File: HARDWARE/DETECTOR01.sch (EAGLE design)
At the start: 6 parts

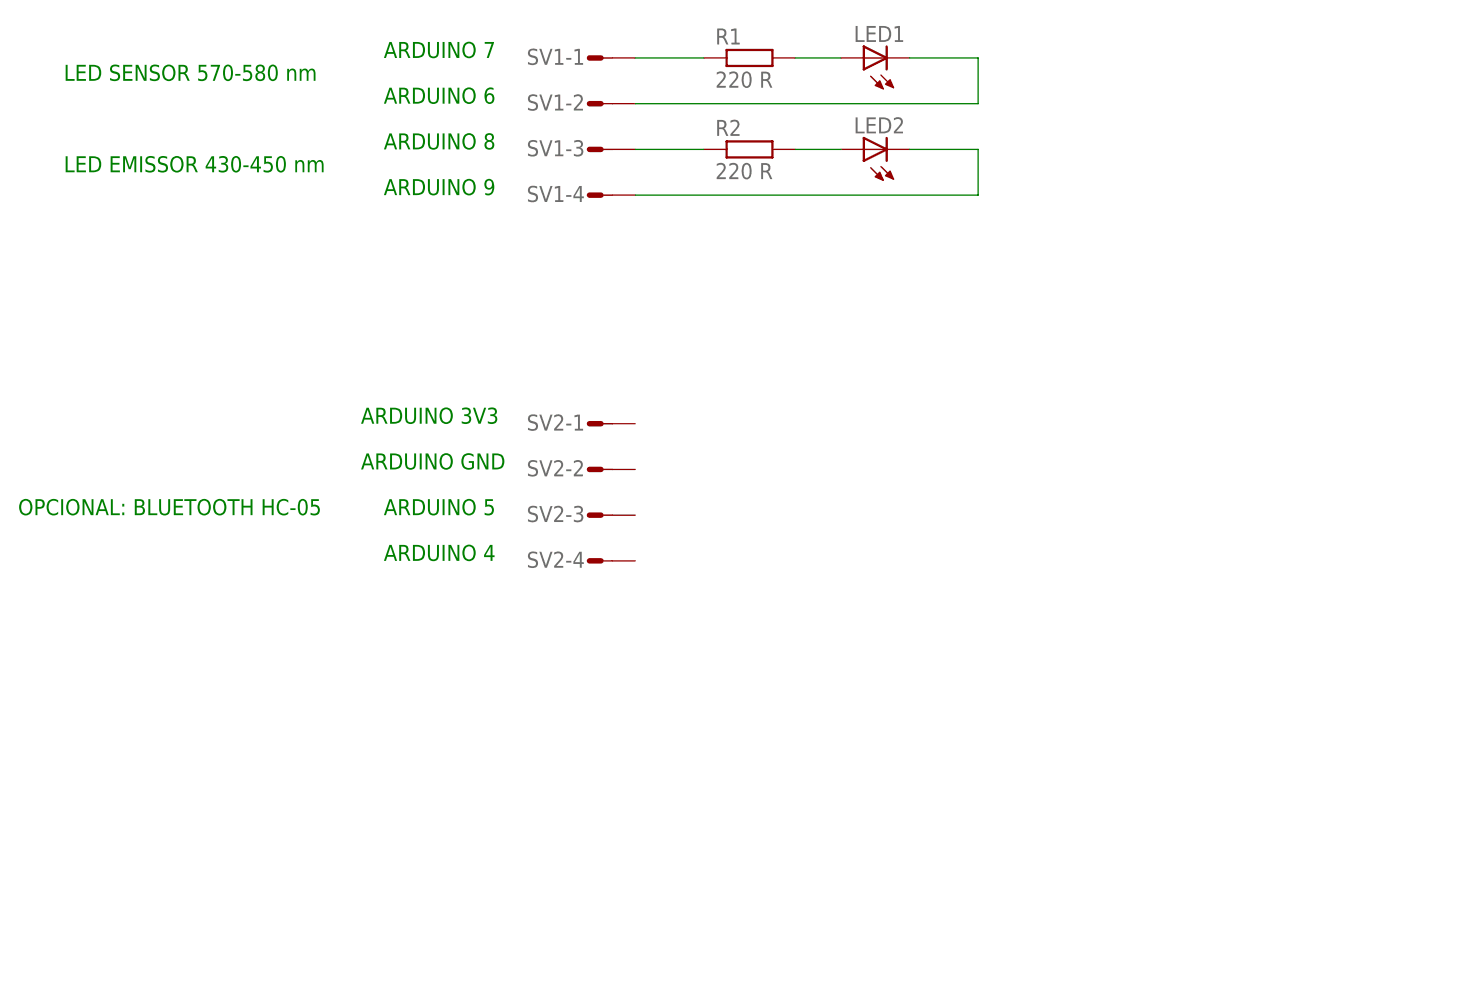
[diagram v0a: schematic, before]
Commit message: Adequações
-proteção ADC
-Correção detector00
-Adição detector05
-Inclusão de teste de tempo de leitura e de conjunto optoeletrônico
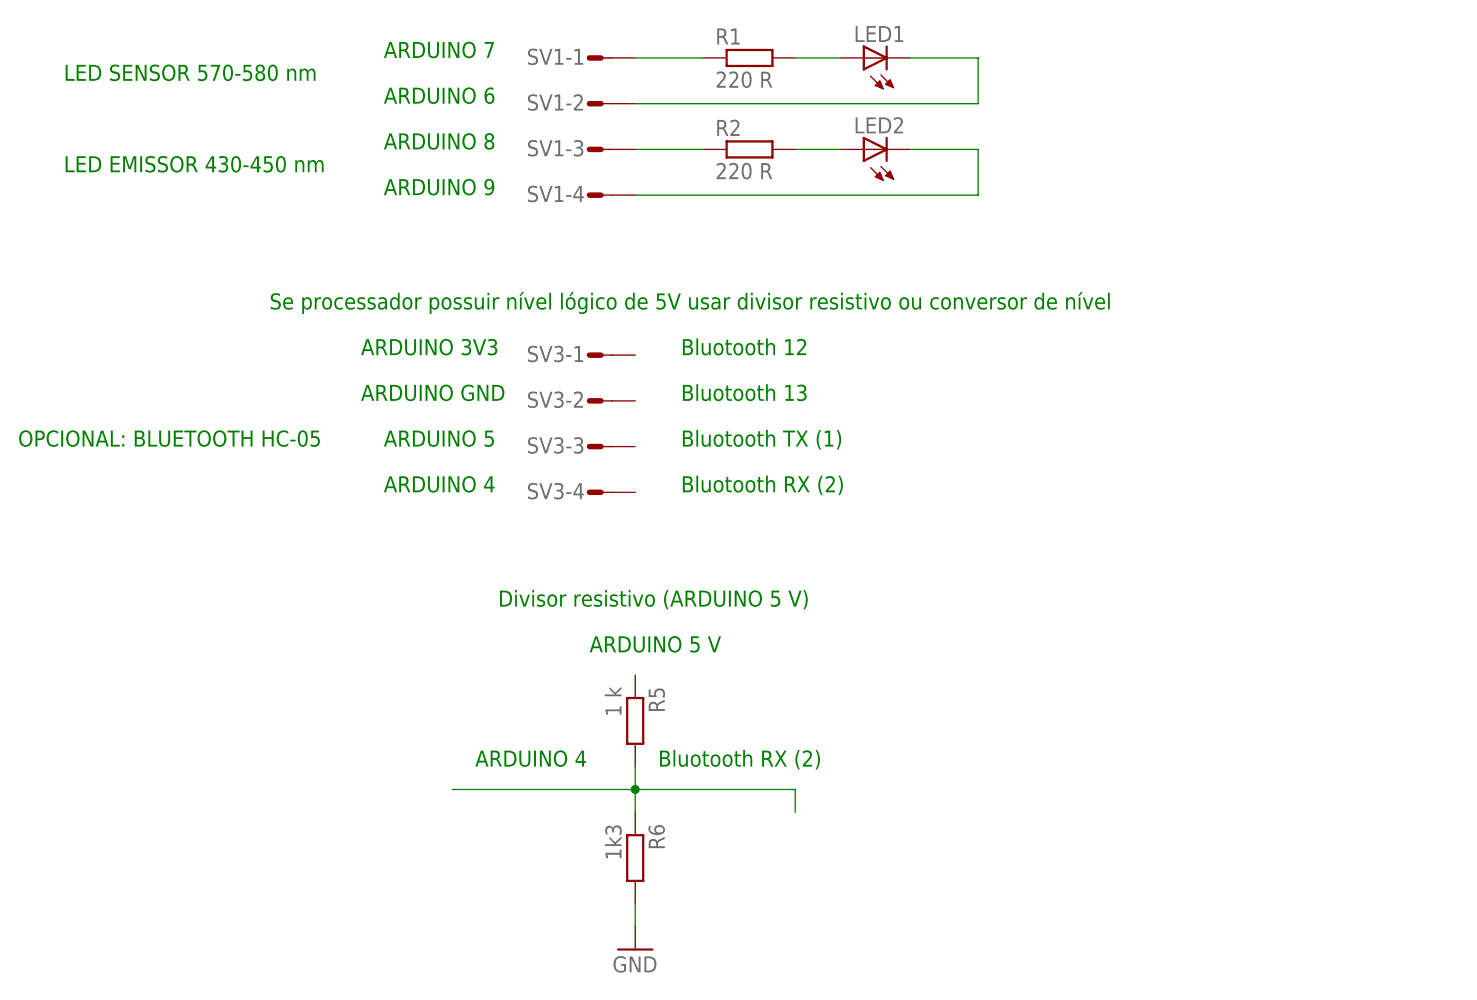
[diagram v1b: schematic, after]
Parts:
- removed SV2: (no value), con-amp-mt:L04P
- added R5: 1 k, rcl:R-EU_0204/7
- added R6: 1k3, rcl:R-EU_0204/7
- added SV3: (no value), con-amp-mt:L04P
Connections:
- new net GND: R6.2
- new net N$7: R5.2, R6.1
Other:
- note added: "ARDUINO 5 V"
- note added: "Bluotooth 12"
- note added: "Bluotooth 13"
- note added: "Bluotooth RX (2)"
- note added: "Bluotooth TX (1)"
- note added: "Divisor resistivo (ARDUINO 5 V)"
- note added: "Se processador possuir nível lógico de 5V usar divisor resistivo ou conversor de nível"
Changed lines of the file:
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@@
 <parts>
 <part name="SV1" library="con-amp-mt" deviceset="L04P" device=""/>
-<part name="SV2" library="con-amp-mt" deviceset="L04P" device=""/>
 <part name="LED1" library="led" deviceset="LED" device="5MM"/>
 <part name="LED2" library="led" deviceset="LED" device="5MM"/>
 <part name="R1" library="rcl" deviceset="R-EU_" device="0204/7" value="220 R"/>
 <part name="R2" library="rcl" deviceset="R-EU_" device="0204/7" value="220 R"/>
+<part name="SV3" library="con-amp-mt" deviceset="L04P" device=""/>
+<part name="R5" library="rcl" deviceset="R-EU_" device="0204/7" value="1 k"/>
+<part name="R6" library="rcl" deviceset="R-EU_" device="0204/7" value="1k3"/>
+<part name="GND5" library="supply1" deviceset="GND" device=""/>
 </parts>
 <sheets>
@@
 <text x="15.24" y="66.04" size="1.778" layer="91">ARDUINO 8</text>
 <text x="15.24" y="60.96" size="1.778" layer="91">ARDUINO 9</text>
-<text x="12.7" y="35.56" size="1.778" layer="91">ARDUINO 3V3</text>
-<text x="12.7" y="30.48" size="1.778" layer="91">ARDUINO GND</text>
-<text x="15.24" y="25.4" size="1.778" layer="91">ARDUINO 5</text>
-<text x="15.24" y="20.32" size="1.778" layer="91">ARDUINO 4</text>
-<text x="-25.4" y="25.4" size="1.778" layer="91">OPCIONAL: BLUETOOTH HC-05</text>
 <text x="-20.32" y="73.66" size="1.778" layer="91">LED SENSOR 570-580 nm</text>
 <text x="-20.32" y="63.5" size="1.778" layer="91">LED EMISSOR 430-450 nm</text>
+<text x="12.7" y="43.18" size="1.778" layer="91">ARDUINO 3V3</text>
+<text x="12.7" y="38.1" size="1.778" layer="91">ARDUINO GND</text>
+<text x="15.24" y="33.02" size="1.778" layer="91">ARDUINO 5</text>
+<text x="15.24" y="27.94" size="1.778" layer="91">ARDUINO 4</text>
+<text x="-25.4" y="33.02" size="1.778" layer="91">OPCIONAL: BLUETOOTH HC-05</text>
+<text x="48.26" y="43.18" size="1.778" layer="91">Bluotooth 12</text>
+<text x="48.26" y="38.1" size="1.778" layer="91">Bluotooth 13</text>
+<text x="48.26" y="33.02" size="1.778" layer="91">Bluotooth TX (1)</text>
+<text x="48.26" y="27.94" size="1.778" layer="91">Bluotooth RX (2)</text>
+<text x="2.54" y="48.26" size="1.778" layer="91">Se processador possuir nível lógico de 5V usar divisor resistivo ou conversor de nível</text>
+<text x="38.1" y="10.16" size="1.778" layer="91">ARDUINO 5 V</text>
+<text x="25.4" y="-2.54" size="1.778" layer="91">ARDUINO 4</text>
+<text x="45.72" y="-2.54" size="1.778" layer="91">Bluotooth RX (2)</text>
+<text x="27.94" y="15.24" size="1.778" layer="91">Divisor resistivo (ARDUINO 5 V)</text>
 </plain>
 <instances>
@@
 <instance part="SV1" gate="-3" x="38.1" y="66.04"/>
 <instance part="SV1" gate="-4" x="38.1" y="60.96"/>
-<instance part="SV2" gate="-1" x="38.1" y="35.56"/>
-<instance part="SV2" gate="-2" x="38.1" y="30.48"/>
-<instance part="SV2" gate="-3" x="38.1" y="25.4"/>
-<instance part="SV2" gate="-4" x="38.1" y="20.32"/>
 <instance part="LED1" gate="G$1" x="68.58" y="76.2" rot="R90"/>
 <instance part="LED2" gate="G$1" x="68.58" y="66.04" rot="R90"/>
 <instance part="R1" gate="G$1" x="55.88" y="76.2"/>
 <instance part="R2" gate="G$1" x="55.88" y="66.04"/>
+<instance part="SV3" gate="-1" x="38.1" y="43.18"/>
+<instance part="SV3" gate="-2" x="38.1" y="38.1"/>
+<instance part="SV3" gate="-3" x="38.1" y="33.02"/>
+<instance part="SV3" gate="-4" x="38.1" y="27.94"/>
+<instance part="R5" gate="G$1" x="43.18" y="2.54" rot="R270"/>
+<instance part="R6" gate="G$1" x="43.18" y="-12.7" rot="R270"/>
+<instance part="GND5" gate="1" x="43.18" y="-22.86"/>
 </instances>
 <busses>
@@
 </segment>
 </net>
+<net name="GND" class="0">
+<segment>
+<pinref part="GND5" gate="1" pin="GND"/>
+<pinref part="R6" gate="G$1" pin="2"/>
+<wire x1="43.18" y1="-20.32" x2="43.18" y2="-17.78" width="0.1524" layer="91"/>
+</segment>
+</net>
+<net name="N$7" class="0">
+<segment>
+<pinref part="R5" gate="G$1" pin="2"/>
+<pinref part="R6" gate="G$1" pin="1"/>
+<wire x1="43.18" y1="-2.54" x2="43.18" y2="-5.08" width="0.1524" layer="91"/>
+<wire x1="43.18" y1="-5.08" x2="43.18" y2="-7.62" width="0.1524" layer="91"/>
+<wire x1="43.18" y1="-5.08" x2="22.86" y2="-5.08" width="0.1524" layer="91"/>
+<junction x="43.18" y="-5.08"/>
+<wire x1="43.18" y1="-5.08" x2="60.96" y2="-5.08" width="0.1524" layer="91"/>
+<wire x1="60.96" y1="-5.08" x2="60.96" y2="-7.62" width="0.1524" layer="91"/>
+</segment>
+</net>
